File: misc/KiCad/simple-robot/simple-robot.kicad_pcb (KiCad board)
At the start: 2 copper layers, 99.8 x 81 mm, 46 parts, among them U1 Pico2

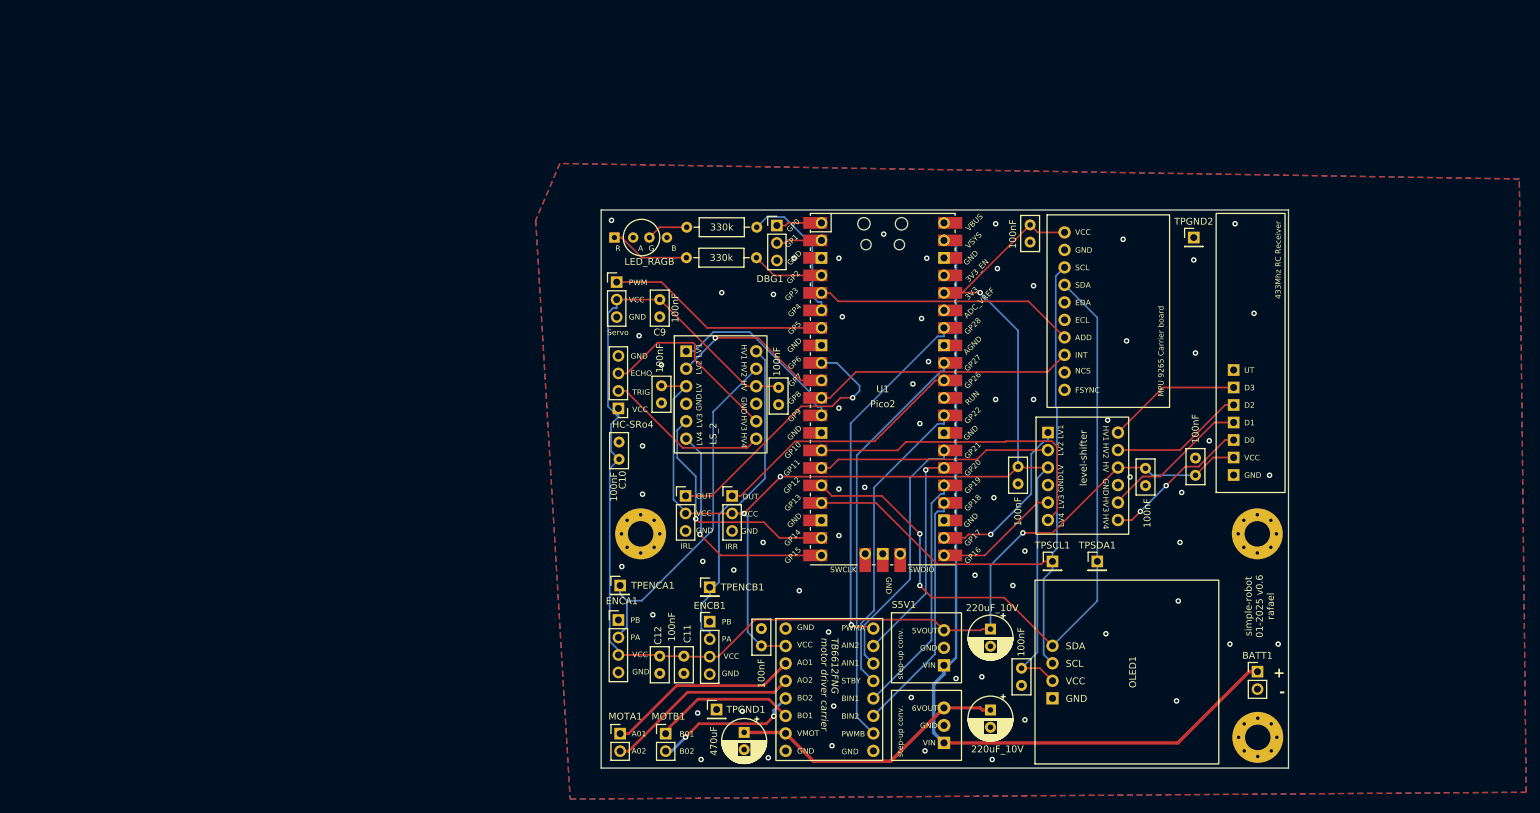
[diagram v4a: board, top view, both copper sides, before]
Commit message: Upgrade KiCad project and refresh footprints
Refresh fp-info-cache with new battery and switch footprints.
Convert PCB to newer KiCad generator/version and update layers,
net names, footprint UUIDs and component positions.
Adjust plot/export and soldermask settings, and tenting.
Update project preferences and DRC/teardrop rules.
Bump schematic date and revision.
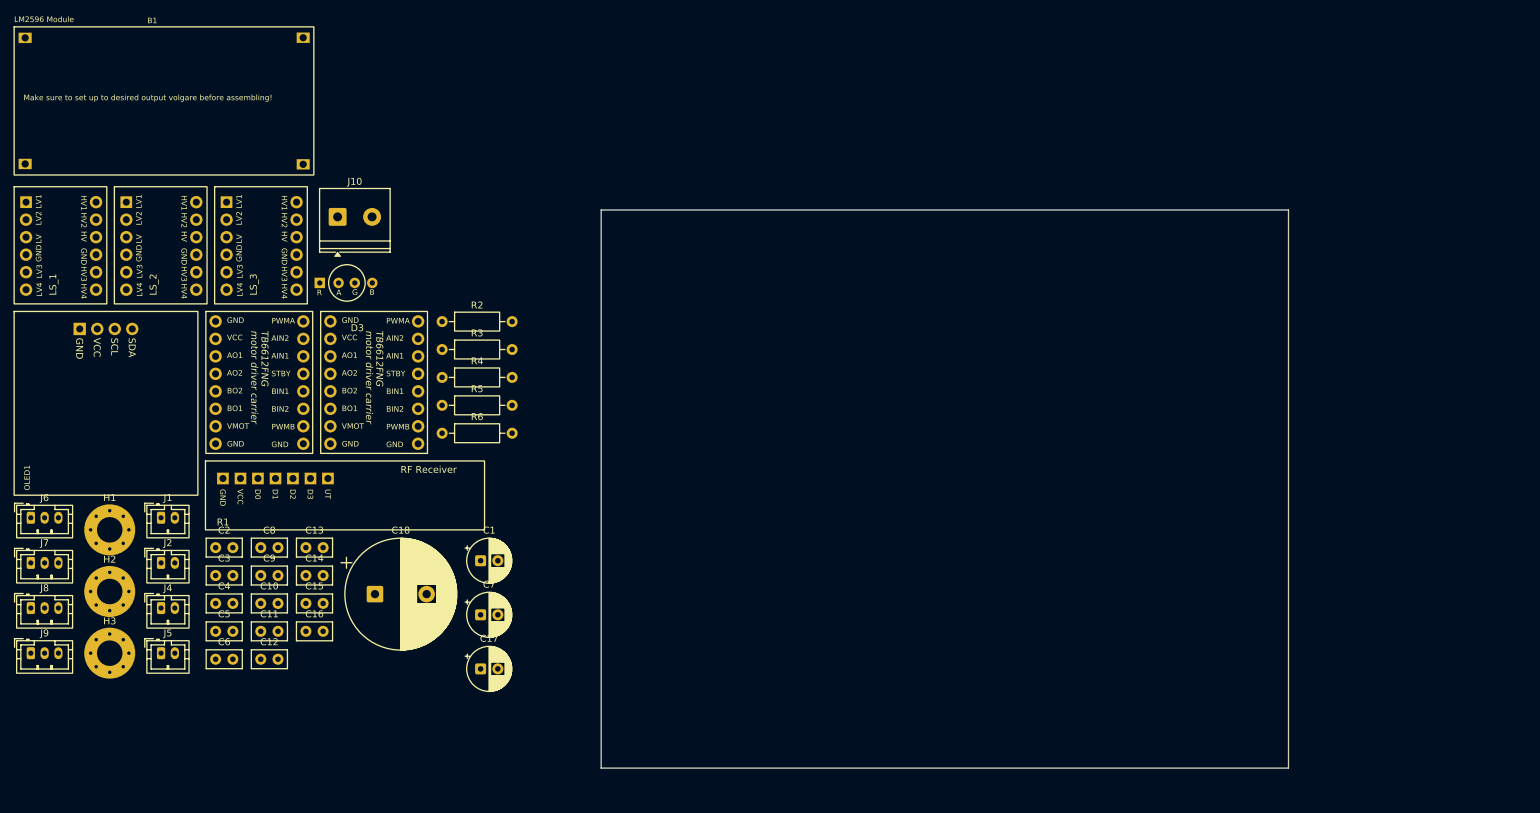
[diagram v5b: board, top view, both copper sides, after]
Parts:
- removed BATT1: Conn_01x02_Pin, Connector_PinHeader_2.54mm:PinHeader_1x02_P2.54mm_Vertical
- removed DBG1, IRL1, IRR1, SERVO1: Conn_01x03_Pin, Connector_PinHeader_2.54mm:PinHeader_1x03_P2.54mm_Vertical
- removed ENCA1, ENCB1, HC-SRo4: Conn_01x04_Pin, Connector_PinHeader_2.54mm:PinHeader_1x04_P2.54mm_Vertical
- removed IMU1: ~, common-hobby-things:MPU 9265 IMU carrier board
- removed MOTA1, MOTB1: ~, Connector_PinHeader_2.54mm:PinHeader_1x02_P2.54mm_Vertical
- removed S5V1: ~, common-hobby-things:Pololu step-up converter 2.5-5.5V in 5V out
- removed S6V1: ~, common-hobby-things:Pololu step-up converter 2.5-5.5V in 6V out
- removed TPENCA1, TPENCB1, TPGND1, TPGND2, TPSCL1, TPSDA1: Conn_01x01_Pin, Connector_PinHeader_2.54mm:PinHeader_1x01_P2.54mm_Vertical
- removed U1: Pico2, MCU_RaspberryPi_and_Boards:RPi_Pico_SMD_TH
- added B1: LM2596 Module, common-hobby-things:LM2596_Module, F.Cu at (-23.2, 27.9)
- added C16: 100nF_Ceramic, Capacitor_THT:C_Disc_D5.0mm_W2.5mm_P2.50mm, F.Cu at (12.1, 119.2)
- added C18: 4700uF_16V, Capacitor_THT:CP_Radial_D16.0mm_P7.50mm, F.Cu at (22.2, 113.8)
- added C7: 220uF, Capacitor_THT:CP_Radial_D6.3mm_P2.50mm, F.Cu at (37.5, 116.8)
- added J1: MotLA, Connector_JST:JST_PH_B2B-PH-K_1x02_P2.00mm_Vertical, F.Cu at (-8.88, 102.7)
- added J10: Screw_Terminal_2_P5.00mm, TerminalBlock_Phoenix:TerminalBlock_Phoenix_PT-1,5-2-5.0-H_1x02_P5.00mm_Horizontal, F.Cu at (16.8, 59.0)
- added J2: MotLB, Connector_JST:JST_PH_B2B-PH-K_1x02_P2.00mm_Vertical, F.Cu at (-8.88, 109.2)
- added J4: MotRA, Connector_JST:JST_PH_B2B-PH-K_1x02_P2.00mm_Vertical, F.Cu at (-8.88, 115.8)
- added J5: MotRB, Connector_JST:JST_PH_B2B-PH-K_1x02_P2.00mm_Vertical, F.Cu at (-8.88, 122.3)
- added J6: ENC_LF, Connector_JST:JST_PH_B3B-PH-K_1x03_P2.00mm_Vertical, F.Cu at (-27.8, 102.7)
- added J7: ENC_LR, Connector_JST:JST_PH_B3B-PH-K_1x03_P2.00mm_Vertical, F.Cu at (-27.8, 109.2)
- added J8: ENC_RF, Connector_JST:JST_PH_B3B-PH-K_1x03_P2.00mm_Vertical, F.Cu at (-27.8, 115.8)
- added J9: ENC_RR, Connector_JST:JST_PH_B3B-PH-K_1x03_P2.00mm_Vertical, F.Cu at (-27.8, 122.3)
- added LS_3: Level Shifter, common-hobby-things:Level shifter 4 bi-dir, F.Cu at (8.25, 67.0)
- added MD2: RightTrack, common-hobby-things:TB6612FNG motor driver carrier, F.Cu at (14.4, 73.0)
- added R4: 20k, Resistor_THT:R_Axial_DIN0207_L6.3mm_D2.5mm_P10.16mm_Horizontal, F.Cu at (31.9, 82.3)
- added R5: 1k, Resistor_THT:R_Axial_DIN0207_L6.3mm_D2.5mm_P10.16mm_Horizontal, F.Cu at (31.9, 86.3)
- added R6: 1k, Resistor_THT:R_Axial_DIN0207_L6.3mm_D2.5mm_P10.16mm_Horizontal, F.Cu at (31.9, 90.4)
- C1: value 470uF -> 220uF
- C10, C11, C13, C14, C15, C3, C4, C5, C6, C8, C9: value 100nF -> 100nF_Ceramic
- C17: value 220uF_10V -> 10uF_10V
- C2: value 220uF_10V -> 100nF_Ceramic; footprint Capacitor_THT:CP_Radial_D6.3mm_P2.50mm -> Capacitor_THT:C_Disc_D5.0mm_W2.5mm_P2.50mm
- LS_1, LS_2: value ~ -> Level Shifter
- MD1: value ~ -> LeftTrack
- R1: value ~ -> RF Receiver
- moved H2 168.0 mm to (-16.3, 113.4)
- moved H3 167.4 mm to (-16.3, 122.3)
- moved LS_1 152.0 mm to (-20.9, 67.0)
- moved OLED1 149.3 mm to (-16.9, 80.3), turned to 0 degrees
- moved C5 144.0 mm to (-0.96, 119.2), turned to 0 degrees
- moved R1 142.0 mm to (7.73, 99.5), turned to 0 degrees
- moved C3 135.8 mm to (-0.96, 111.0), turned to 0 degrees
- moved C4 130.3 mm to (-0.96, 115.1), turned to 0 degrees
- moved C6 117.0 mm to (-0.96, 123.2), turned to 0 degrees
- moved C2 114.9 mm to (-0.96, 107.0), turned to 0 degrees
- moved C8 110.5 mm to (5.59, 107.0), turned to 0 degrees
- moved MD1 94.0 mm to (-2.23, 73.0)
- moved LS_2 84.1 mm to (-6.30, 67.0)
- moved H1 77.1 mm to (-16.3, 104.4)
- moved C17 74.2 mm to (37.5, 124.6), turned to 0 degrees
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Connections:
- C1 pad 1: Net-(MD1-VMOT) -> +VBAT
- C10 pad 1: Net-(ENCA1-Pin_3) -> +5V
- C11 pad 1: GND -> +5V
- C11 pad 2: Net-(ENCA1-Pin_3) -> GND
- C12 pad 1: GND -> +5V
- C12 pad 2: Net-(ENCA1-Pin_3) -> GND
- C13 pad 1: Net-(ENCA1-Pin_3) -> +5V
- C14 pad 1: Net-(IMU1-VCC) -> +5V
- C15 pad 1: Net-(IMU1-VCC) -> +3V3
- C17 pad 1: Net-(ENCA1-Pin_3) -> +5V
- C2 pad 1: Net-(MD1-VMOT) -> GND
- C2 pad 2: GND -> +5V
- C3 pad 1: Net-(ENCA1-Pin_3) -> +5V
- C4 pad 1: Net-(IMU1-VCC) -> +3V3
- C5 pad 1: Net-(ENCA1-Pin_3) -> +5V
- C6 pad 2: Net-(IMU1-VCC) -> +3V3
- C8 pad 1: Net-(IMU1-VCC) -> +3V3
- C9 pad 1: Net-(ENCA1-Pin_3) -> GND
- C9 pad 2: GND -> +3V3
- LS_1 pad 1: Net-(LS_1-LV1) -> RC_D
- LS_1 pad 2: Net-(LS_1-LV2) -> RC_C
- LS_1 pad 3: Net-(IMU1-VCC) -> +3V3
- LS_1 pad 5: Net-(LS_1-LV3) -> RC_B
- LS_1 pad 6: Net-(LS_1-LV4) -> RC_A
- LS_1 pad 9: Net-(ENCA1-Pin_3) -> +5V
- LS_2 pad 1: Net-(LS_2-LV1) -> ENC_LF
- LS_2 pad 2: Net-(LS_2-LV2) -> ENC_LR
- LS_2 pad 3: Net-(IMU1-VCC) -> +3V3
- LS_2 pad 5: Net-(LS_2-LV3) -> ENC_RF
- LS_2 pad 6: Net-(LS_2-LV4) -> ENC_RR
- LS_2 pad 9: Net-(ENCA1-Pin_3) -> +5V
- MD1 pad 10: Net-(MD1-AIN2) -> LMOT_F_REV
- MD1 pad 11: Net-(MD1-AIN1) -> LMOT_F_FWD
- MD1 pad 12: Net-(MD1-STBY) -> LMOT_STB
- MD1 pad 13: Net-(MD1-BIN1) -> LMOT_R_FWD
- MD1 pad 14: Net-(MD1-BIN2) -> LMOT_R_REV
- MD1 pad 15: Net-(MD1-PWMB) -> M_LR_PWM
- MD1 pad 16: unconnected-(MD1-GND-Pad16) -> GND
- MD1 pad 2: Net-(IMU1-VCC) -> +3V3
- MD1 pad 7: Net-(MD1-VMOT) -> +VBAT
- MD1 pad 9: Net-(MD1-PWMA) -> M_LF_PWM
- OLED1 pad 2: Net-(IMU1-VCC) -> +3V3
- OLED1 pad 3: Net-(IMU1-SCL) -> I2C SCL
- OLED1 pad 4: Net-(IMU1-SDA) -> I2C SDA
- R1 pad 2: Net-(ENCA1-Pin_3) -> +5V
- R2 pad 1: Net-(U1-GPIO2) -> unconnected-(R2-Pad1)
- R3 pad 1: Net-(U1-GPIO4) -> unconnected-(R3-Pad1)
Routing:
- net Net-(IMU1-VCC): track 195.5 -> 0.00 mm, vias 3 -> 0
- net Net-(ENCA1-Pin_3): track 194.1 -> 0.00 mm, vias 1 -> 0
- net +3V8: track 126.9 -> 0.00 mm
- net Net-(IMU1-SDA): track 104.6 -> 0.00 mm, vias 2 -> 0
- net Net-(IMU1-SCL): track 96.8 -> 0.00 mm
- net Net-(MD1-PWMB): track 60.3 -> 0.00 mm
- net Net-(MD1-PWMA): track 52.7 -> 0.00 mm, vias 1 -> 0
- net Net-(J7-SIG): track 51.2 -> 0.00 mm
- net Net-(J6-SIG): track 48.7 -> 0.00 mm
- net Net-(LS_1-LV4): track 46.3 -> 0.00 mm
- net Net-(MD1-STBY): track 44.8 -> 0.00 mm
- net Net-(MD1-VMOT): track 40.8 -> 0.00 mm
- net Net-(IRL1-Pin_1): track 39.2 -> 0.00 mm, vias 1 -> 0
- net Net-(IMU1-ADD): track 38.0 -> 0.00 mm
- net Net-(IMU1-INT): track 37.9 -> 0.00 mm
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- removed copper zone on B.Cu, net GND
- removed copper zone on F.Cu, net GND
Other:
- board text removed: "+"
- board text removed: "-"
- board text removed: "433Mhz RC Receiver"
- board text removed: "A01"
- board text removed: "A02"
- board text removed: "B01"
- board text removed: "B02"
- board text removed: "ECHO"
- board text removed: "GND"
- board text removed: "IRL"
- board text removed: "IRR"
- board text removed: "MPU 9265 Carrier board"
- board text removed: "OUT"
- board text removed: "PA"
- board text removed: "PB"
- board text removed: "PWM"
- board text removed: "Servo"
- board text removed: "TRIG"
- board text removed: "VCC"
- board text removed: "level-shifter"
- board text removed: "simple-robot 01-2025 v0.6 rafael"

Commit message: Reintroduce components and let clippy run rampage (#15)
* merge

* Update KiCad schematic to include all connections and IC

Make KiCad PCB 4-layer and update footprints

* Add string helper module for status text

Provide status_text that converts &str to heapless::String<20>.
Returns None and logs a warning if the input exceeds capacity.

* Add 47ohm resistor and reposition schematic parts

Add new PCM_SL_Resistors:47ohm symbol and instantiate R3
Reposition rotary encoder, GV_TX/GV_RX and several power/GND
symbols; add short wires and junctions to reconnect traces

* most things re-introduced, schematic and code match

* Document per-component licenses and clean README

* Remove motion monitor task and pin assignments

* Migrate flash storage to sequential-storage v7

Update code to use MapStorage/MapConfig and new fetch_item/store_item
APIs. Adjust Value::deserialize_from to return (Self, usize).
Enable inactivity tracker task; bump hcsr04_async and other deps.
Expand BOM in README

* Add JST connectors, rename nets, update footprints

Rename power net +VBAT to +BATT and label several previously
unconnected nets (e.g. IR_OBST, GV_TX/GV_RX, Net-(D1-A), Net-(D3-A),
and various Jx pins). Add JST RF_PWR (J16) and RF_Logic (J15)
symbols to the schematic. Replace/adjust footprint and properties for
the capacitor/MD1 component and update reference/value/metadata.

* Silence unused warnings and tidy imports

Prefix unused parameters and variables with `_`; remove unused imports
and Signal objects; add #[allow(clippy::cast_possible_truncation)]
for STORAGE_OFFSET; remove unnecessary `mut` on the flash parameter.

* cleaning

* Update PCB layout: move footprints and pads

Update fp-info-cache (new hash) and add PCA9555 entry
Reposition many footprints and adjust silk text rotations/UUIDs
Change pad defaults (drill 2.8, width 3.2) and board prefs
(active layer and visible layers)

* Replace 2-pin JST with 4-pin and reposition parts

* pcb routing and some cleaning up; makin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
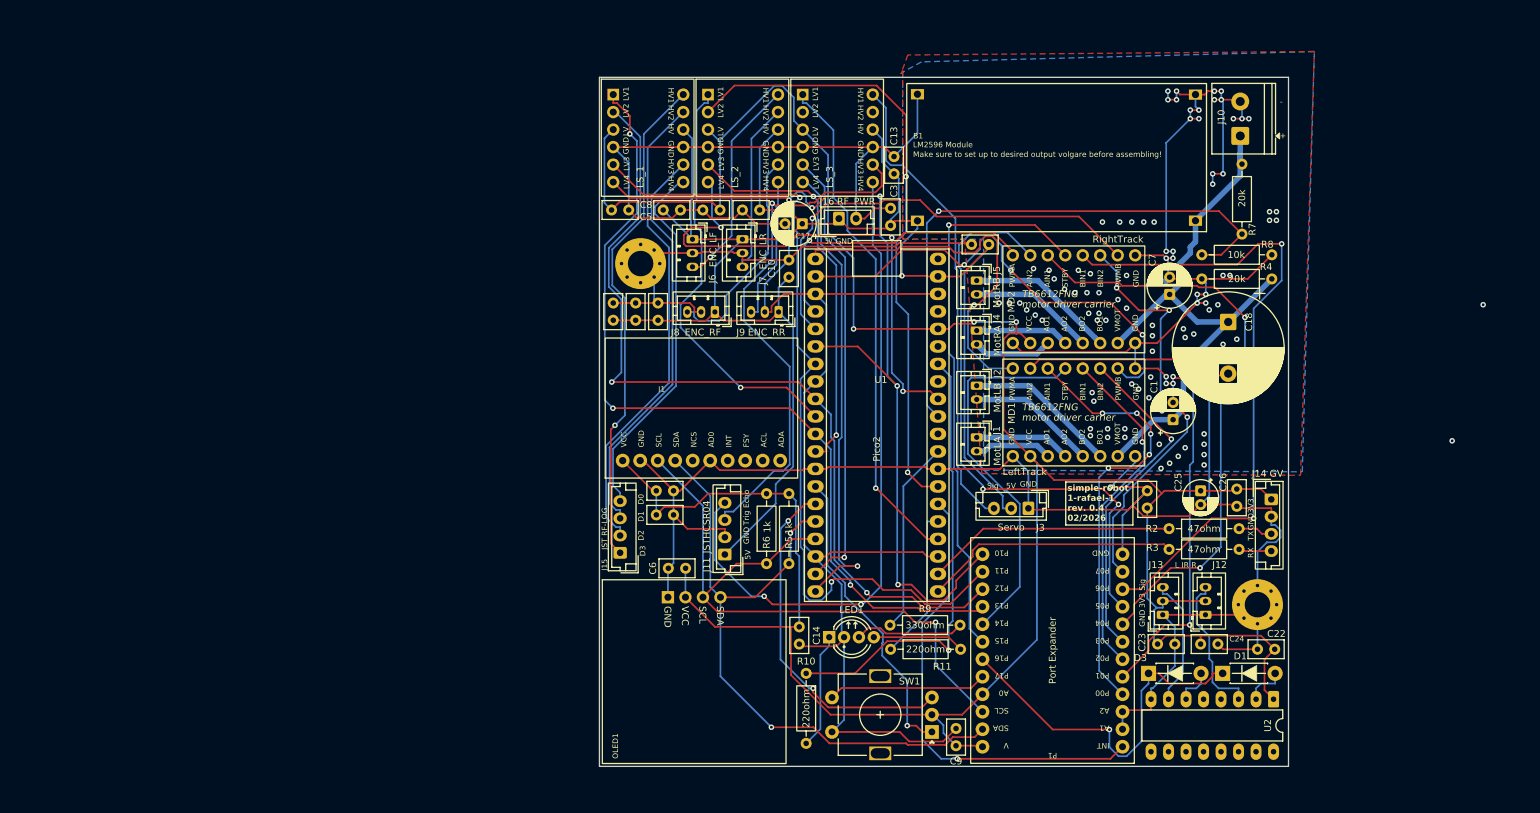
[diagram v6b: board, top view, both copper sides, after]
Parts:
- removed H3: MountingHole_Pad, MountingHole:MountingHole_3.7mm_Pad_Via
- removed R1: RF Receiver, common-hobby-things:433Mhz RC Receiver
- added C19: 100nF_Ceramic, Capacitor_THT:C_Disc_D5.0mm_W2.5mm_P2.50mm, F.Cu at (134.2, 101.2)
- added C20: 100nF_Ceramic, Capacitor_THT:C_Disc_D5.0mm_W2.5mm_P2.50mm, F.Cu at (75.5, 58.0)
- added C21: 100nF_Ceramic, Capacitor_THT:C_Disc_D5.0mm_W2.5mm_P2.50mm, F.Cu at (69.8, 58.0)
- added C22: 100nF_Ceramic, Capacitor_THT:C_Disc_D5.0mm_W2.5mm_P2.50mm, F.Cu at (150.2, 121.8)
- added C23: 100nF_Ceramic, Capacitor_THT:C_Disc_D5.0mm_W2.5mm_P2.50mm, F.Cu at (135.8, 121.0)
- added C24: 100nF_Ceramic, Capacitor_THT:C_Disc_D5.0mm_W2.5mm_P2.50mm, F.Cu at (142.0, 121.0)
- added C25: 10uF_16V, Capacitor_THT:CP_Radial_D5.0mm_P2.00mm, F.Cu at (142.0, 98.8)
- added C26: 100nF_Ceramic, Capacitor_THT:C_Disc_D5.0mm_W2.5mm_P2.50mm, F.Cu at (147.2, 98.5)
- added D1: 1N5819, PCM_Diode_THT_AKL:D_DO-41_SOD81_P7.62mm_Horizontal, F.Cu at (145.2, 125.2)
- added I1: ~, common-hobby-things:ICM-20948-module, F.Cu at (50.5, 86.8)
- added J11: JSTHCSR04, Connector_JST:JST_EH_B4B-EH-A_1x04_P2.50mm_Vertical, F.Cu at (73.0, 108.0)
- added J12: IR_RF, Connector_JST:JST_PH_B3B-PH-K_1x03_P2.00mm_Vertical, F.Cu at (142.7, 116.8)
- added J13: IR_LF, Connector_JST:JST_PH_B3B-PH-K_1x03_P2.00mm_Vertical, F.Cu at (136.5, 116.8)
- added J14: GV, Connector_JST:JST_EH_B4B-EH-A_1x04_P2.50mm_Vertical, F.Cu at (152.2, 100.0)
- added J15: JST RF-LOG, Connector_JST:JST_EH_B4B-EH-A_1x04_P2.50mm_Vertical, F.Cu at (57.8, 107.8)
- added J16: RF_PWR, Connector_JST:JST_EH_B2B-EH-A_1x02_P2.50mm_Vertical, F.Cu at (89.5, 59.2)
- added J3: Servo, Connector_JST:JST_EH_B3B-EH-A_1x03_P2.50mm_Vertical, F.Cu at (117.0, 101.3)
- added LED1: LED_5mm_RGB_Kcom_RKGB, PCM_LED_THT_AKL:LED_D5.0mm-4_RGB_Wide_Pins, F.Cu at (88.1, 120.0)
- added P1: Port Expander, common-hobby-things:PCA9555 Port Expander, F.Cu at (120.5, 142.2)
- added R10: 220ohm, Resistor_THT:R_Axial_DIN0207_L6.3mm_D2.5mm_P10.16mm_Horizontal, F.Cu at (84.8, 125.2)
- added R11: 220ohm, Resistor_THT:R_Axial_DIN0207_L6.3mm_D2.5mm_P10.16mm_Horizontal, F.Cu at (97.0, 121.8)
- added R7: 20k, Resistor_THT:R_Axial_DIN0207_L6.3mm_D2.5mm_P10.16mm_Horizontal, F.Cu at (148.0, 61.5)
- added R8: 10k, Resistor_THT:R_Axial_DIN0207_L6.3mm_D2.5mm_P10.16mm_Horizontal, F.Cu at (152.3, 64.5)
- added R9: 330ohm, Resistor_THT:R_Axial_DIN0207_L6.3mm_D2.5mm_P10.16mm_Horizontal, F.Cu at (96.9, 118.2)
- added SW1: RotaryEncoder_Switch, Rotary_Encoder:RotaryEncoder_Alps_EC11E-Switch_Vertical_H20mm, F.Cu at (103.0, 133.8)
- added U1: Pico2, PCM_SL_Development_Boards:raspberry_pi_pico_THT, F.Cu at (86.1, 65.1)
- added U2: CD4049UB, Package_DIP:DIP-16_W7.62mm_LongPads, F.Cu at (152.6, 129.0)
- D3: value LED_RAGB -> 1N5819; footprint common-hobby-things:LED RAGB -> PCM_Diode_THT_AKL:D_DO-41_SOD81_P7.62mm_Horizontal
- R2, R3: value 330k -> 47ohm
- moved H1 166.9 mm to (150.2, 115.3)
- moved B1 163.2 mm to (135.8, 64.7), turned to 180 degrees
- moved J10 131.5 mm to (147.8, 47.2), turned to 90 degrees
- moved J5 130.1 mm to (109.5, 68.2), turned to -90 degrees
- moved C18 130.0 mm to (146.0, 74.2), turned to -90 degrees
- moved D3 127.9 mm to (134.4, 125.2)
- moved J4 125.0 mm to (109.5, 75.5), turned to -90 degrees
- moved R4 121.3 mm to (152.3, 68.0), turned to 180 degrees
- moved J2 121.1 mm to (109.5, 83.5), turned to -90 degrees
- moved J9 119.3 mm to (80.8, 72.8), turned to 180 degrees
- moved J1 118.9 mm to (109.5, 91.0), turned to -90 degrees
- moved C2 118.2 mm to (108.8, 63.0)
- moved MD1 117.9 mm to (113.5, 95.0), turned to 90 degrees
- moved J7 113.5 mm to (75.5, 62.2), turned to -90 degrees
- moved C3 110.3 mm to (97.0, 60.2), turned to 90 degrees
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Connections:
- net +VBAT renamed +BATT
- C14 pad 1: +5V -> +3V3
- D3 pad 1: Net-(D3-RK) -> IR_OBST
- D3 pad 2: GND -> Net-(D3-A)
- LS_3 pad 1: unconnected-(LS_3-LV1-Pad1) -> US_SERVO
- LS_3 pad 11: unconnected-(LS_3-HV3-Pad11) -> Net-(LS_3-HV3)
- LS_3 pad 12: unconnected-(LS_3-HV4-Pad12) -> Net-(LS_3-HV4)
- LS_3 pad 3: unconnected-(LS_3-LV-Pad3) -> +3V3
- LS_3 pad 5: unconnected-(LS_3-LV3-Pad5) -> US_ECHO
- LS_3 pad 6: unconnected-(LS_3-LV4-Pad6) -> US_TRIG
- LS_3 pad 7: unconnected-(LS_3-HV1-Pad7) -> Net-(LS_3-HV1)
- LS_3 pad 9: unconnected-(LS_3-HV-Pad9) -> +5V
- MD1 pad 5: Net-(J2-+) -> Net-(J2--)
- MD1 pad 6: Net-(J2--) -> Net-(J2-+)
- MD2 pad 5: Net-(J5-+) -> Net-(J5--)
- MD2 pad 6: Net-(J5--) -> Net-(J5-+)
- R2 pad 1: unconnected-(R2-Pad1) -> GV_TX
- R2 pad 2: Net-(D3-RK) -> Net-(J14-Pad3)
- R3 pad 1: unconnected-(R3-Pad1) -> GV_RX
- R3 pad 2: Net-(D3-GK) -> Net-(J14-Pad4)
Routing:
- net GND: track 0.00 -> 753.9 mm, vias 0 -> 102
- net +3V3: track 0.00 -> 400.4 mm, vias 0 -> 3
- net +5V: track 0.00 -> 244.0 mm, vias 0 -> 1
- net RC_A: track 0.00 -> 130.7 mm, vias 0 -> 5
- net RC_D: track 0.00 -> 125.6 mm, vias 0 -> 3
- net RC_C: track 0.00 -> 124.8 mm, vias 0 -> 2
- net RC_B: track 0.00 -> 121.1 mm, vias 0 -> 2
- net I2C SDA: track 0.00 -> 97.9 mm, vias 0 -> 2
- net Net-(LS_3-HV4): track 0.00 -> 95.9 mm, vias 0 -> 2
- net RMOT_R_FWD: track 0.00 -> 95.5 mm, vias 0 -> 2
- net I2C SCL: track 0.00 -> 93.5 mm, vias 0 -> 1
- net ENC_LR: track 0.00 -> 90.6 mm, vias 0 -> 2
- net RMOT_F_FWD: track 0.00 -> 86.7 mm, vias 0 -> 2
- net +BATT: track 0.00 -> 86.2 mm
- net RMOT_F_REV: track 0.00 -> 86.1 mm, vias 0 -> 2
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- added copper zone on In2.Cu, net +3V3
- added copper zone on In2.Cu, net +5V
- added copper zone on B.Cu, net GND
- added copper zone on F.Cu, net GND
- added copper zone on In1.Cu, net GND
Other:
- board size 99.8 x 81 mm -> 100 x 100 mm
- copper layers 2 -> 4
- board text added: "+"
- board text added: "-"
- board text added: "3V3"
- board text added: "5V"
- board text added: "D0"
- board text added: "D1"
- board text added: "D2"
- board text added: "D3"
- board text added: "Echo"
- board text added: "GND"
- board text added: "L IR R"
- board text added: "RX"
- board text added: "Sig"
- board text added: "TX"
- board text added: "Trig"
- board text added: "simple-robot 1-rafael-1 rev. 0.4 02/2026"
